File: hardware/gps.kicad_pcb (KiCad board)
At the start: 2 copper layers, 30 x 35 mm, 31 parts, among them P1 CON-SENSOR, P2 U.FL, U1 M24C64, U2 FireFlyX1, U3 DRILL, U4 DRILL, U5 DRILL, U6 DRILL

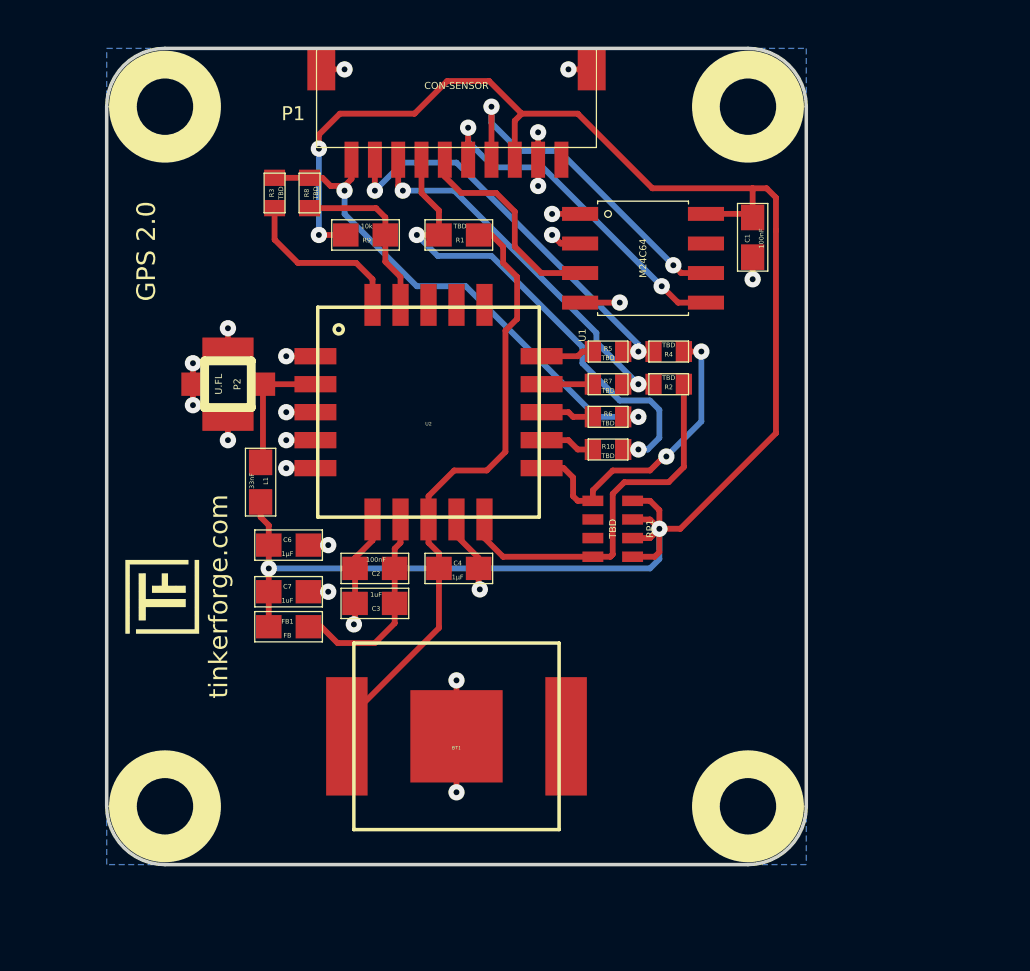
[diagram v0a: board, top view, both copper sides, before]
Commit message: adding hardware prototype for new version with co-processor
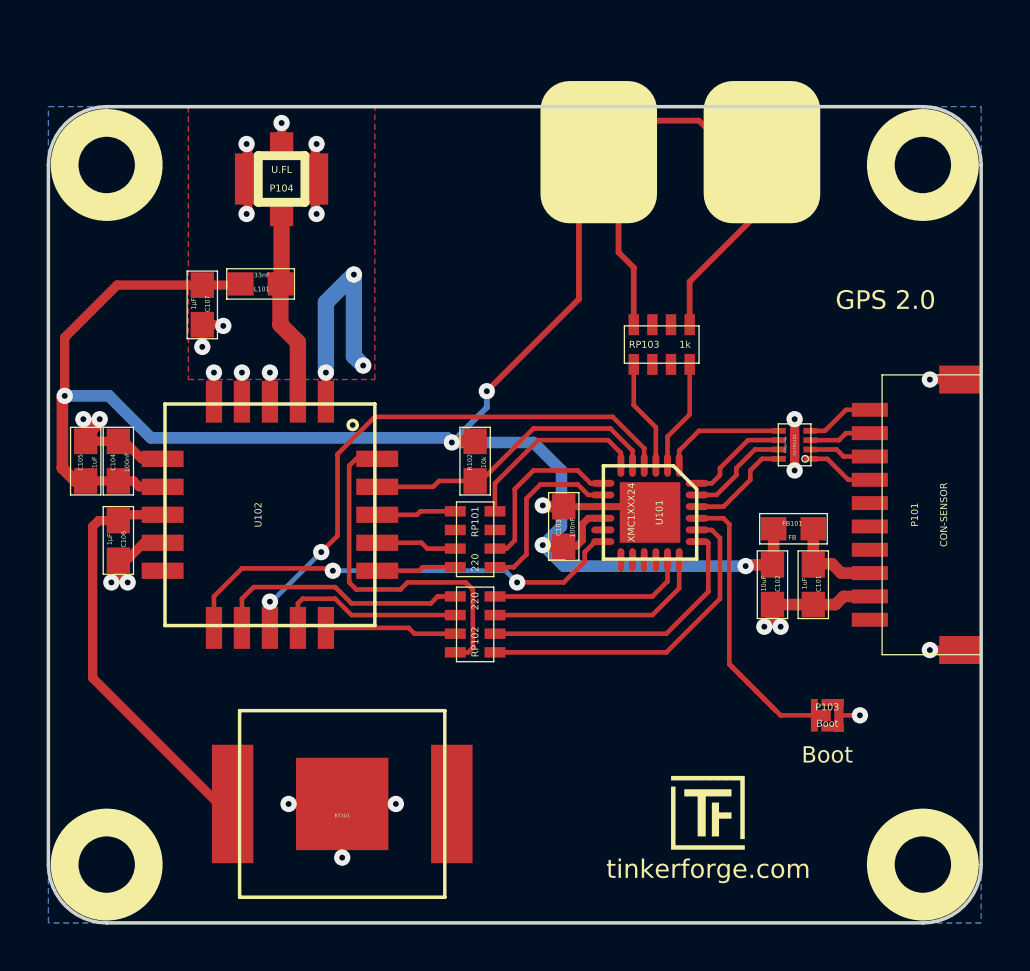
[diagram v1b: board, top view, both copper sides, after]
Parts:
- removed BT1: Battery, kicad-libraries:BATTERY_HOLDER_2998
- removed C1, C2: 100nF, kicad-libraries:0603E
- removed C3, C7: 1uF, kicad-libraries:0603E
- removed C4, C6: 1µF, kicad-libraries:0603E
- removed FB1: FB, kicad-libraries:0603E
- removed the G*** at (183.9, 95.9)
- removed L1: 33nF, kicad-libraries:0603E
- removed P1: CON-SENSOR, kicad-libraries:CON-SENSOR
- removed P2: U.FL, kicad-libraries:U.FL-CON
- removed R1: TBD, kicad-libraries:0603E
- removed R10, R2, R3, R4, R5, R6, R7, R8: TBD, kicad-libraries:0402E
- removed R9: 10k, kicad-libraries:0603E
- removed RP1: TBD, kicad-libraries:4X0603
- removed U1: M24C64, kicad-libraries:SOIC8
- removed U2: FireFlyX1, kicad-libraries:FireFlyX1
- removed U3, U4, U5, U6: DRILL, kicad-libraries:DRILL_NP
- added BT101: Battery, kicad-libraries:BATTERY_HOLDER_2998, F.Cu at (179.0, 115.8)
- added C101: 1uF, kicad-libraries:0603E, F.Cu at (199.2, 106.4)
- added C102: 10uF, kicad-libraries:0603E, F.Cu at (197.4, 106.4)
- added C103: 100nF, kicad-libraries:0603E, F.Cu at (188.5, 103.9)
- added C104: 100nF, kicad-libraries:0603E, F.Cu at (169.4, 101.1)
- added C105: 1uF, kicad-libraries:0603E, F.Cu at (168.0, 101.1)
- added C106: 1µF, kicad-libraries:0603E, F.Cu at (169.4, 104.5)
- added C107: 1µF, kicad-libraries:0603E, F.Cu at (173.0, 94.4)
- added D101: LED blue, kicad-libraries:D0603E, F.Cu at (197.0, 87.6)
- added D102: LED green, kicad-libraries:D0603E, F.Cu at (190.0, 87.6)
- added FB101: FB, kicad-libraries:0603E, F.Cu at (198.3, 104.0)
- added FILTER101: Filter-4x, DFN8-17x135, F.Cu at (198.4, 100.4)
- added L101: 33nF, kicad-libraries:0603E, F.Cu at (175.5, 93.5)
- added P101: CON-SENSOR, kicad-libraries:CON-SENSOR, F.Cu at (206.4, 103.4)
- added P103: Boot, kicad-libraries:SolderJumper, F.Cu at (199.8, 112.0)
- added P104: U.FL, kicad-libraries:U.FL-CON, F.Cu at (176.4, 89.0)
- added R102: 10k, 0603E, F.Cu at (184.7, 101.1)
- added RP101: 220, kicad-libraries:0603X4, F.Cu at (184.7, 104.5)
- added RP102: 220, kicad-libraries:0603X4, F.Cu at (184.7, 108.1)
- added RP103: 1k, kicad-libraries:0603X4, F.Cu at (192.7, 96.1)
- added U101: XMC1XXX24, kicad-libraries:QFN24-4x4mm-0.5mm, F.Cu at (192.2, 103.3)
- added U102: FireFlyX1, kicad-libraries:FireFlyX1, F.Cu at (175.9, 103.4)
- added U103: DRILL, kicad-libraries:DRILL_NP, F.Cu at (203.9, 88.4)
- added U104: DRILL, kicad-libraries:DRILL_NP, F.Cu at (203.9, 118.4)
- added U105: DRILL, kicad-libraries:DRILL_NP, F.Cu at (168.9, 88.4)
- added U106: DRILL, kicad-libraries:DRILL_NP, F.Cu at (168.9, 118.4)
- added VAL: WEEE_7mm_back, kicad-libraries:WEEE_7mm_back, B.Cu at (193.9, 103.4)
- moved G*** 24.2 mm to (193.1, 114.6), turned to 0 degrees
- moved VAL 5.59 mm to (178.9, 103.4), turned to 180 degrees
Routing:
- net GND: track 33.0 -> 62.1 mm, vias 22 -> 28
- net INT: track 0.00 -> 23.8 mm, vias 0 -> 2
- net Net-(P1-Pad10): track 22.4 -> 0.00 mm, vias 2 -> 0
- net Net-(P1-Pad7): track 21.4 -> 0.00 mm, vias 2 -> 0
- net RTCM: track 0.00 -> 20.1 mm, vias 0 -> 2
- net Net-(P1-Pad9): track 18.0 -> 0.00 mm, vias 2 -> 0
- net Net-(P1-Pad8): track 16.5 -> 0.00 mm, vias 2 -> 0
- net Net-(R2-Pad2): track 16.3 -> 0.00 mm
- net Net-(RP102-Pad4): track 0.00 -> 15.3 mm
- net Net-(P103-Pad2): track 0.00 -> 15.3 mm
- net SDA: track 15.0 -> 0.00 mm, vias 2 -> 0
- net SCL: track 14.8 -> 0.00 mm, vias 2 -> 0
- net M-CS: track 0.00 -> 14.3 mm
- net Net-(R4-Pad2): track 13.3 -> 0.00 mm, vias 2 -> 0
- net RESET: track 0.00 -> 13.0 mm
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- added copper zone on F.Cu, net GND
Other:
- board size 30 x 35 mm -> 40 x 35 mm
- net class Default: clearance 0.2 -> 0.15
- rule pad_to_mask_clearance: 0.2 -> 0
- rule trace_clearance: 0.2 -> 0.15
- board text added: "Boot"
- board text added: "Fix"
- board text added: "Status"

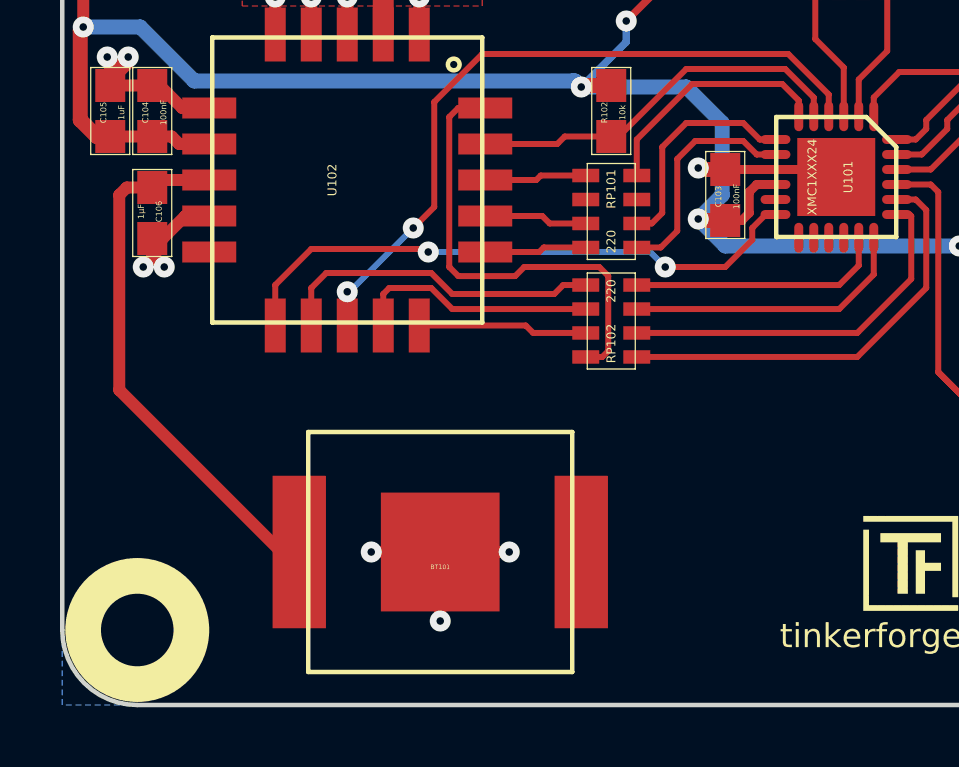
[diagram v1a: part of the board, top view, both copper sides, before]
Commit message: change battery holder to version for cr-1025
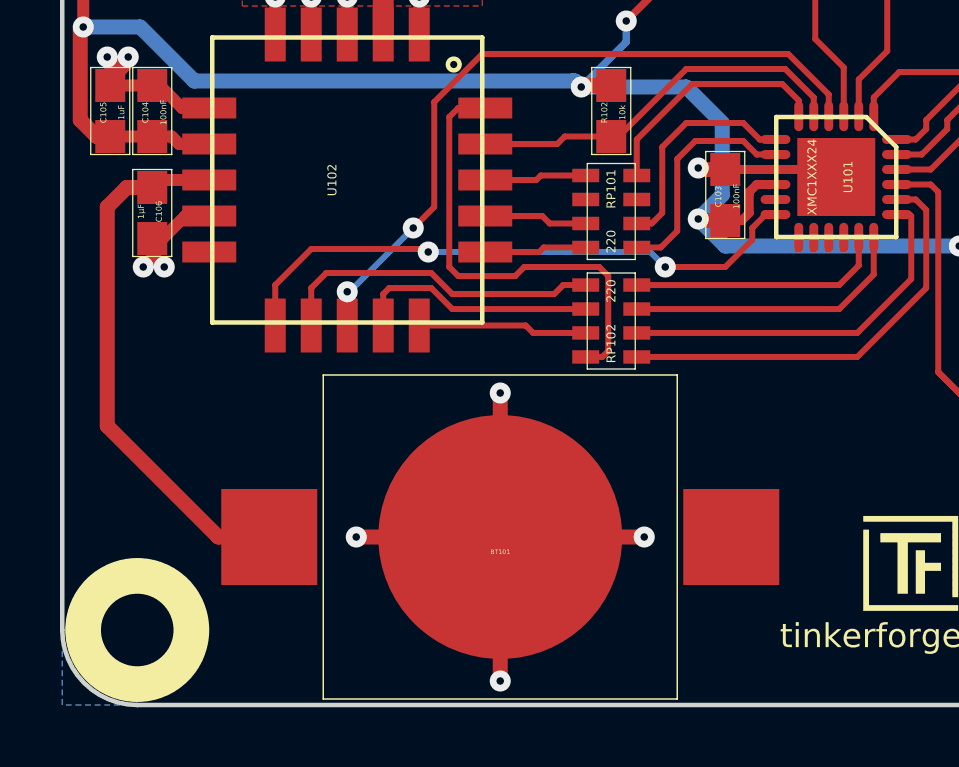
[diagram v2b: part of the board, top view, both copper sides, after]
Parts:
- BT101: footprint kicad-libraries:BATTERY_HOLDER_2998 -> kicad-libraries:BATTERY_HOLDER_BK870
- FILTER101: footprint DFN8-17x135 -> kicad-libraries:DFN8-17x135
- R102: footprint 0603E -> kicad-libraries:0603E
- moved BT101 2.06 mm to (181.0, 115.3)
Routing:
- net GND: track 62.1 -> 74.4 mm, vias 28 -> 29
- net +BATT: track 17.9 -> 19.5 mm

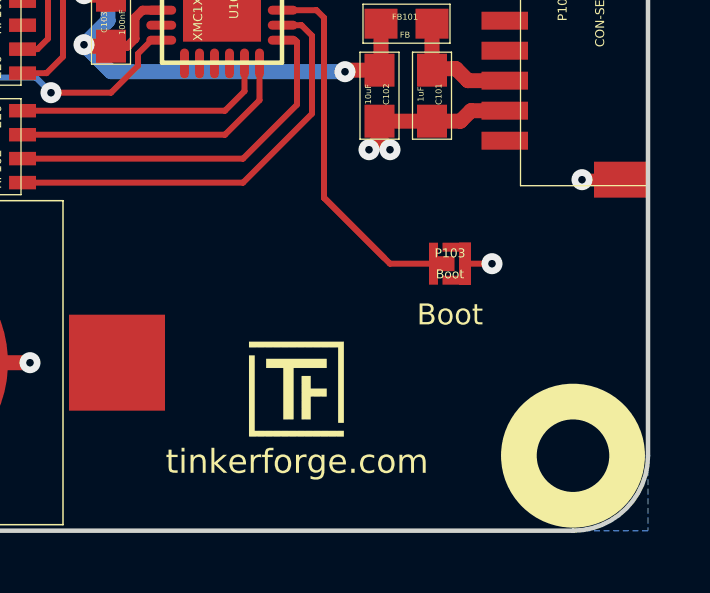
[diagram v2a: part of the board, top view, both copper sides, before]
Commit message: remove boot description
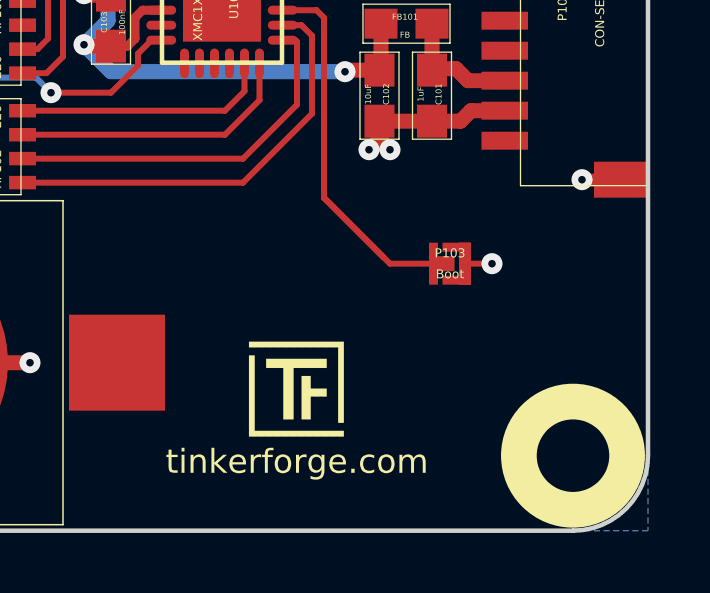
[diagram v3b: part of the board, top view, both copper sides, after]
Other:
- board text removed: "Boot"
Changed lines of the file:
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@@
     (links 78)
     (no_connects 1)
-    (area 166.324999 85.824999 206.475001 120.975001)
+    (area 165.544999 84.8 217.39894 121.755001)
     (thickness 1.6)
-    (drawings 13)
+    (drawings 12)
     (tracks 327)
     (zones 0)
@@
   )
   (setup
-    (last_trace_width 0.2)
+    (last_trace_width 0.25)
     (user_trace_width 0.2)
     (user_trace_width 0.25)
@@
     (effects (font (size 0.7 0.7) (thickness 0.15)))
   )
-  (gr_text Boot (at 199.8 113.7) (layer F.SilkS)
-    (effects (font (size 0.7 0.7) (thickness 0.15)))
-  )

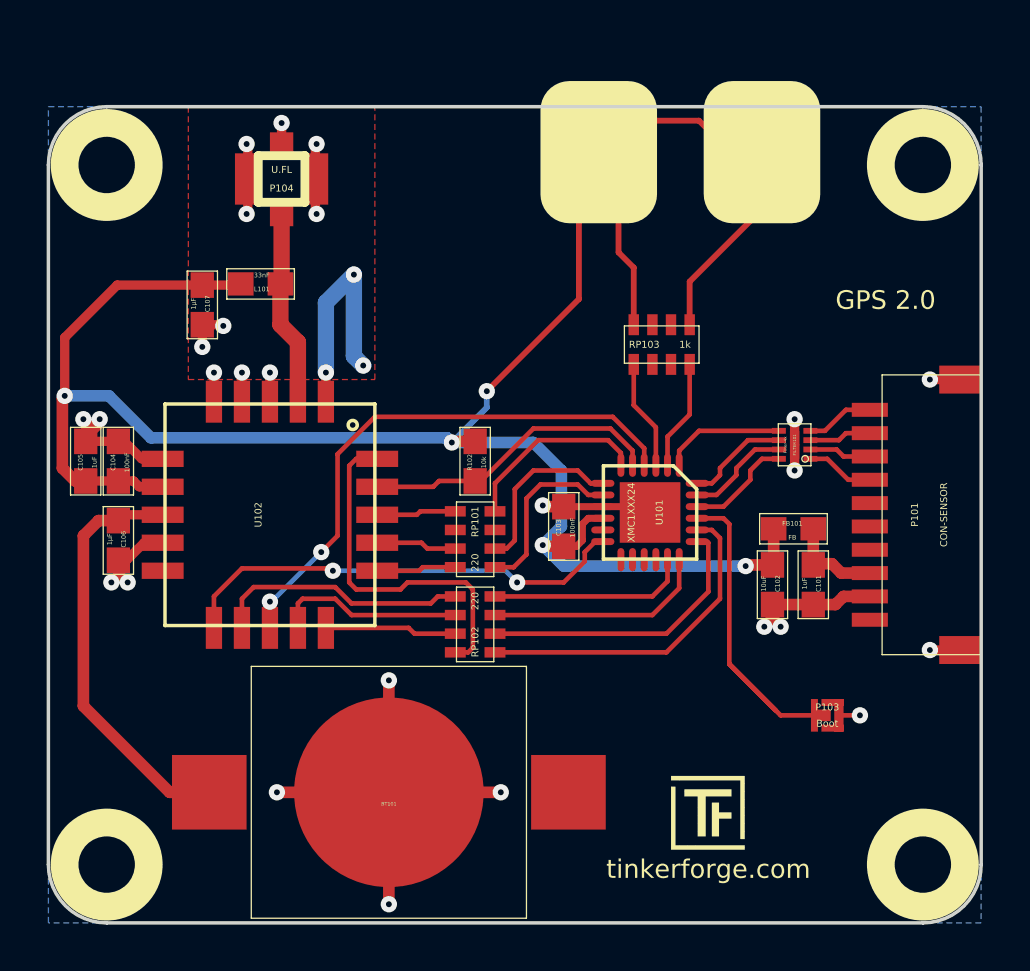
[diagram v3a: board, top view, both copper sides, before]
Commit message: fix pin mapping
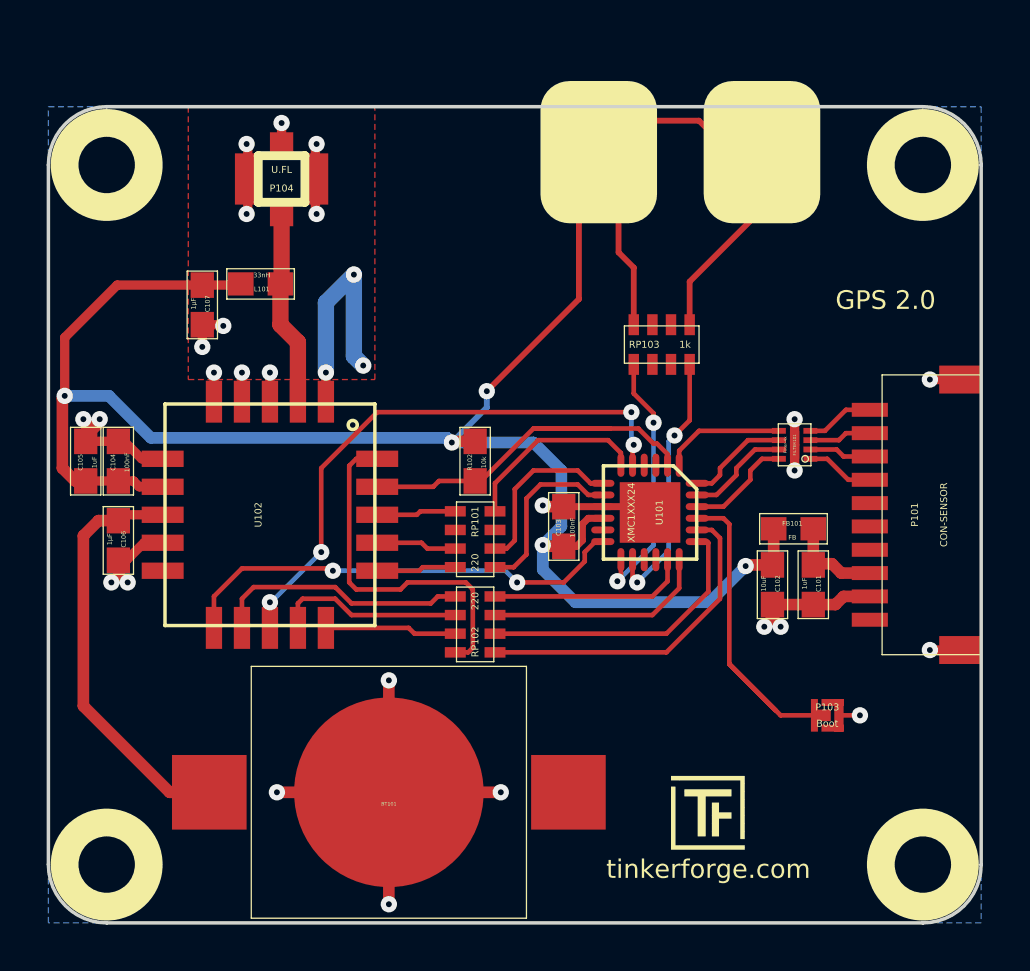
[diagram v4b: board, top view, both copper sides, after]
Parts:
- L101: value 33nF -> 33nH
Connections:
- U101 pad 13: (no net) -> Net-(RP103-Pad5)
- U101 pad 14: (no net) -> Net-(RP103-Pad8)
- U101 pad 2: Net-(RP103-Pad8) -> RESET
- U101 pad 3: Net-(RP103-Pad5) -> (no net)
- U101 pad 4: INT -> (no net)
- U101 pad 5: RESET -> INT
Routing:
- net Net-(RP103-Pad8): track 4.72 -> 11.3 mm, vias 0 -> 2
- net Net-(RP103-Pad5): track 4.72 -> 11.3 mm, vias 0 -> 2
- net RESET: track 13.0 -> 17.7 mm
- net VCC: track 84.6 -> 86.5 mm
- net INT: track 23.8 -> 24.4 mm, vias 2 -> 4

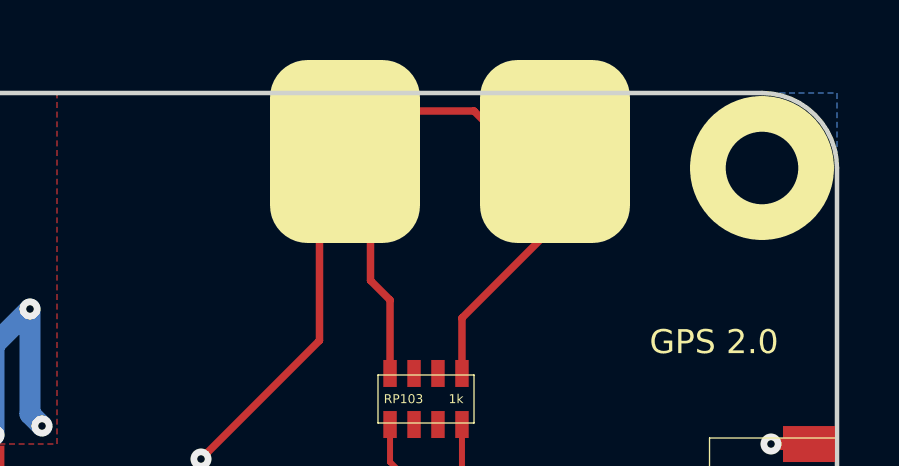
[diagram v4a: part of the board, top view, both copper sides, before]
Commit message: remove silkscreen areas around leds
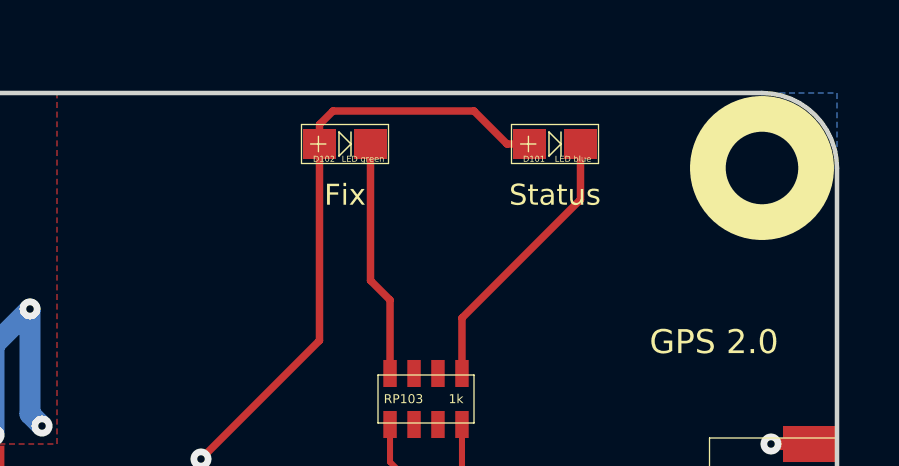
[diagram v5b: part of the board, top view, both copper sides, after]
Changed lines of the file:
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@@
     (links 78)
     (no_connects 1)
-    (area 166.324999 85.824999 206.475001 120.975001)
+    (area 165.544999 84.8 207.255001 121.755001)
     (thickness 1.6)
     (drawings 12)
@@
   (layers
     (0 F.Cu signal)
-    (31 B.Cu signal)
+    (31 B.Cu signal hide)
     (32 B.Adhes user)
     (33 F.Adhes user hide)
@@
   )
   (setup
-    (last_trace_width 0.2)
+    (last_trace_width 0.25)
     (user_trace_width 0.2)
     (user_trace_width 0.25)
@@
       (net 10 RESET))
   )
-  (gr_text Fix (at 190 89.3) (layer F.Mask)
+  (gr_text Fix (at 190 89.3) (layer F.SilkS)
     (effects (font (size 0.7 0.7) (thickness 0.15)))
   )
-  (gr_text Status (at 197 89.3) (layer F.Mask)
+  (gr_text Status (at 197 89.3) (layer F.SilkS)
     (effects (font (size 0.7 0.7) (thickness 0.15)))
   )
@@
       )
     )
-  )
-  (zone (net 0) (net_name "") (layer F.SilkS) (hatch full 0.508)
-    (connect_pads yes (clearance 0.15))
-    (min_thickness 2.5)
-    (fill yes (arc_segments 16) (thermal_gap 0.508) (thermal_bridge_width 0.508))
-    (polygon
-      (pts
-        (xy 194.5 84.8) (xy 194.5 90.9) (xy 199.5 90.9) (xy 199.5 84.8)
-      )
-    )
-  )
-  (zone (net 0) (net_name "") (layer F.SilkS) (hatch full 0.508)
-    (connect_pads yes (clearance 0.15))
-    (min_thickness 2.5)
-    (fill yes (arc_segments 16) (thermal_gap 0.508) (thermal_bridge_width 0.508))
-    (polygon
-      (pts
-        (xy 187.5 84.8) (xy 187.5 90.9) (xy 192.5 90.9) (xy 192.5 84.8)
-      )
-    )
